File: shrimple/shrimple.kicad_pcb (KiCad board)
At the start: 2 copper layers, 249.2 x 105.6 mm, 117 parts, among them U2 SN74LV1T34DCK, U3 Pro Micro RP2040

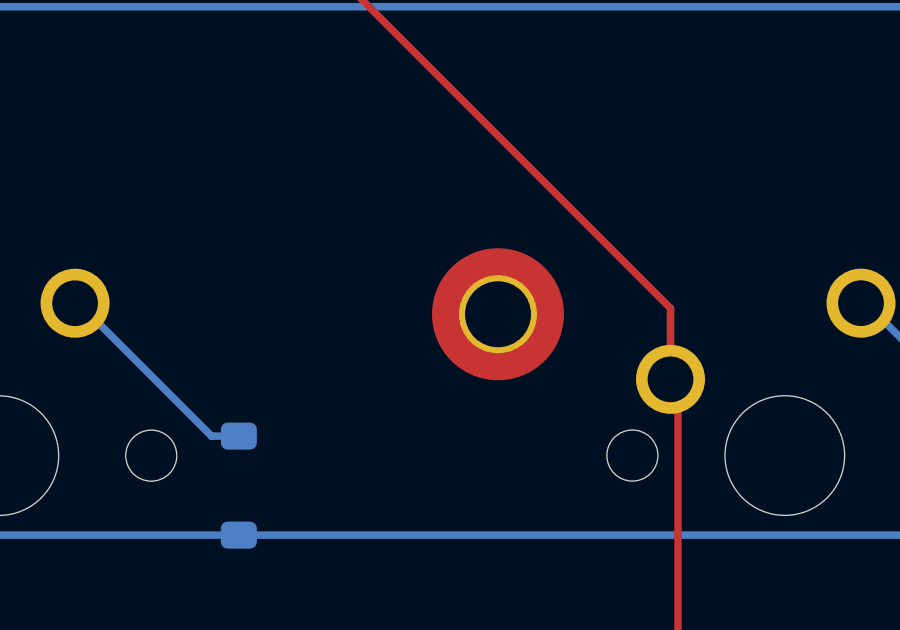
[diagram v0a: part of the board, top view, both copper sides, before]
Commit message: moved mounting hole, updated gerbers
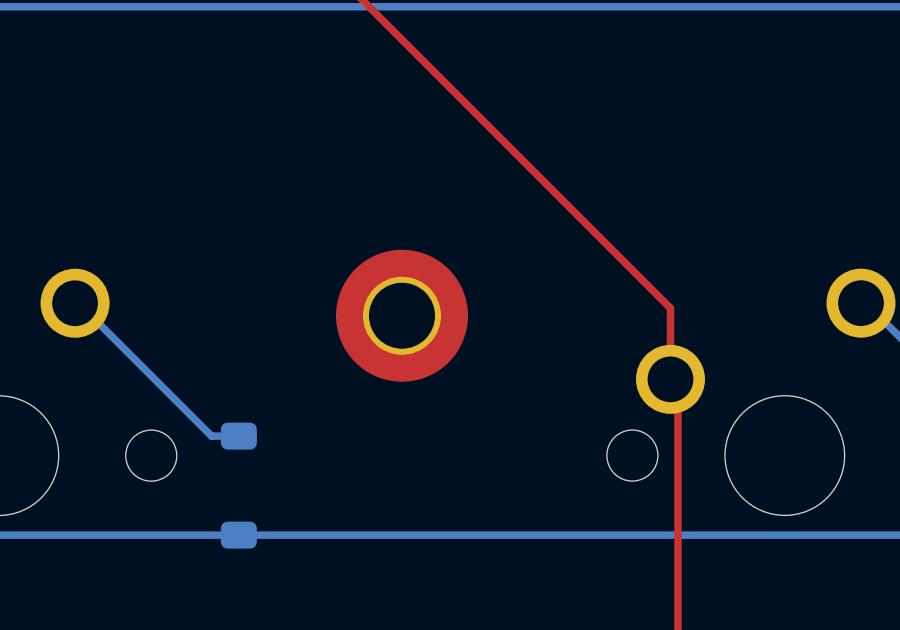
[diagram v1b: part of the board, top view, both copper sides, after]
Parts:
- moved H5 3.20 mm to (246.8, 76.3)
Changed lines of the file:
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@@
 	(footprint "MountingHole:MountingHole_2.2mm_M2_Pad_TopOnly"
 		(layer "F.Cu")
-		(at 250 76.25)
+		(at 246.8 76.3)
 		(descr "Mounting Hole 2.2mm, M2")
 		(tags "mounting hole 2.2mm m2")
@@
 		)
 		(fp_text user "${REFERENCE}"
-			(at 0 0 360)
-			(layer "F.Fab")
-			(effects
+			(at 0 0 0)
+			(layer "F.Fab")
+			(effects
